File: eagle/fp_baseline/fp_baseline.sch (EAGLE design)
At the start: 6 parts, among them J5 TSM-105-01-S-SV

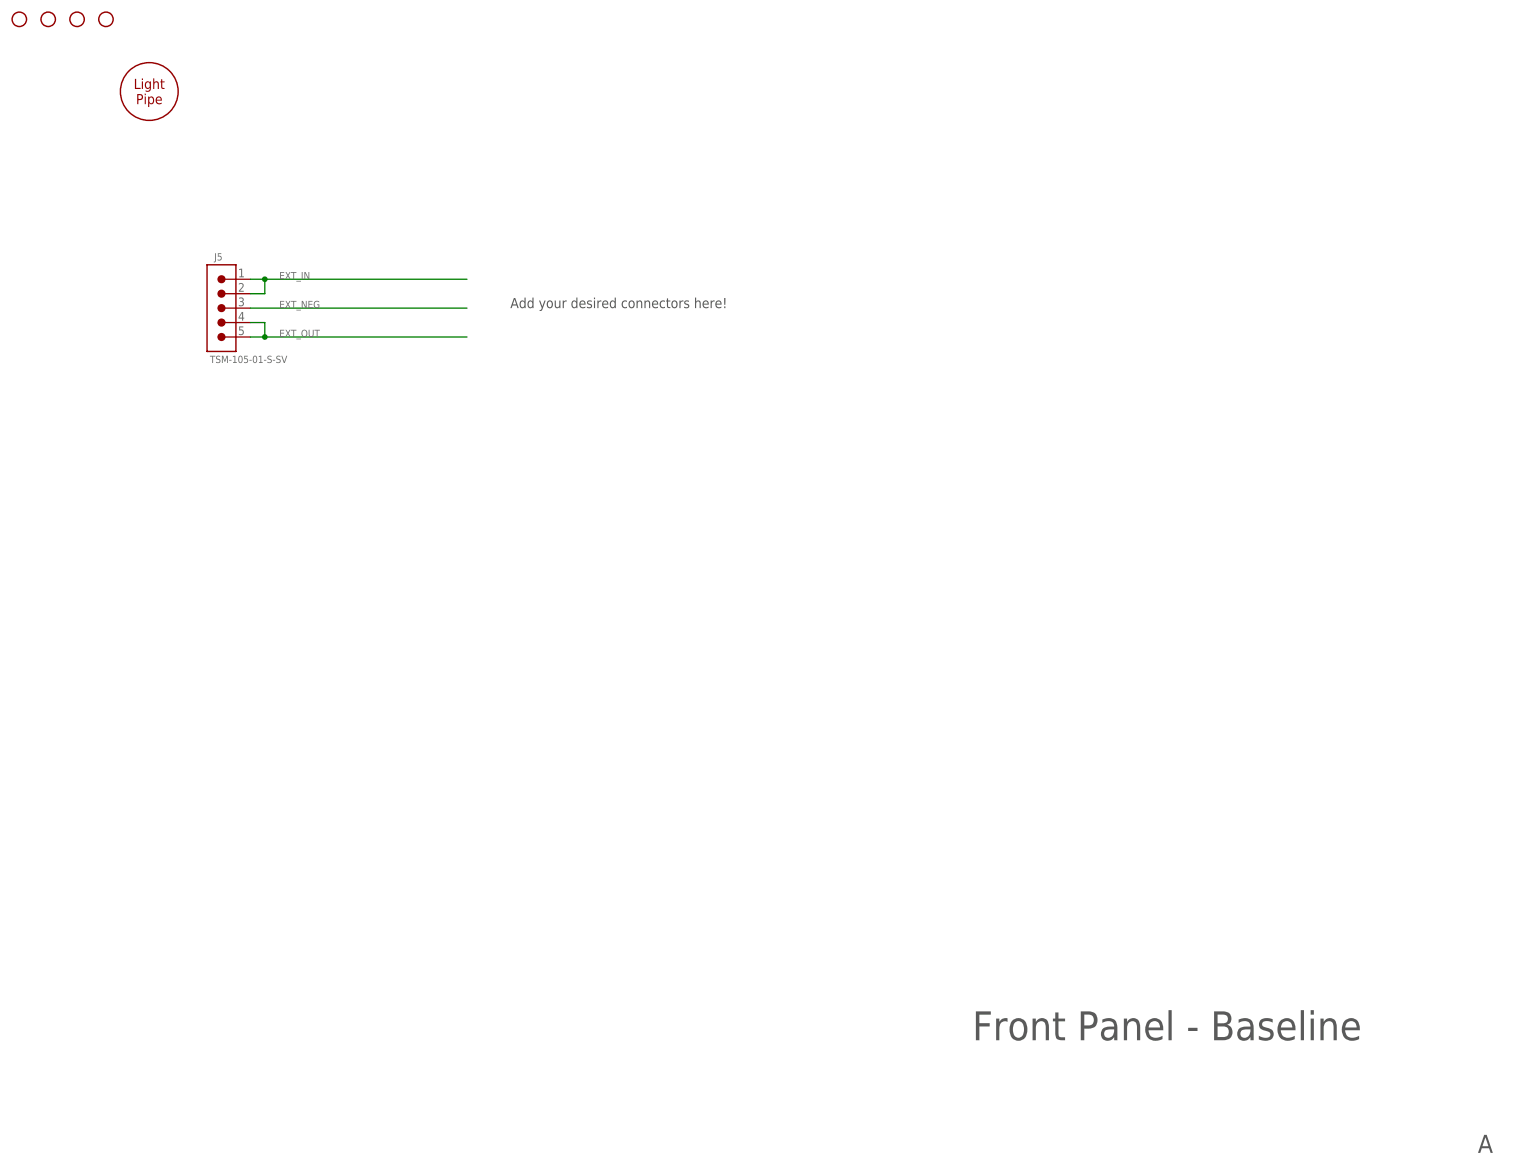
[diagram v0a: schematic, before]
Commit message: Updated baseline to clarify dimensions, placement and part numbers.
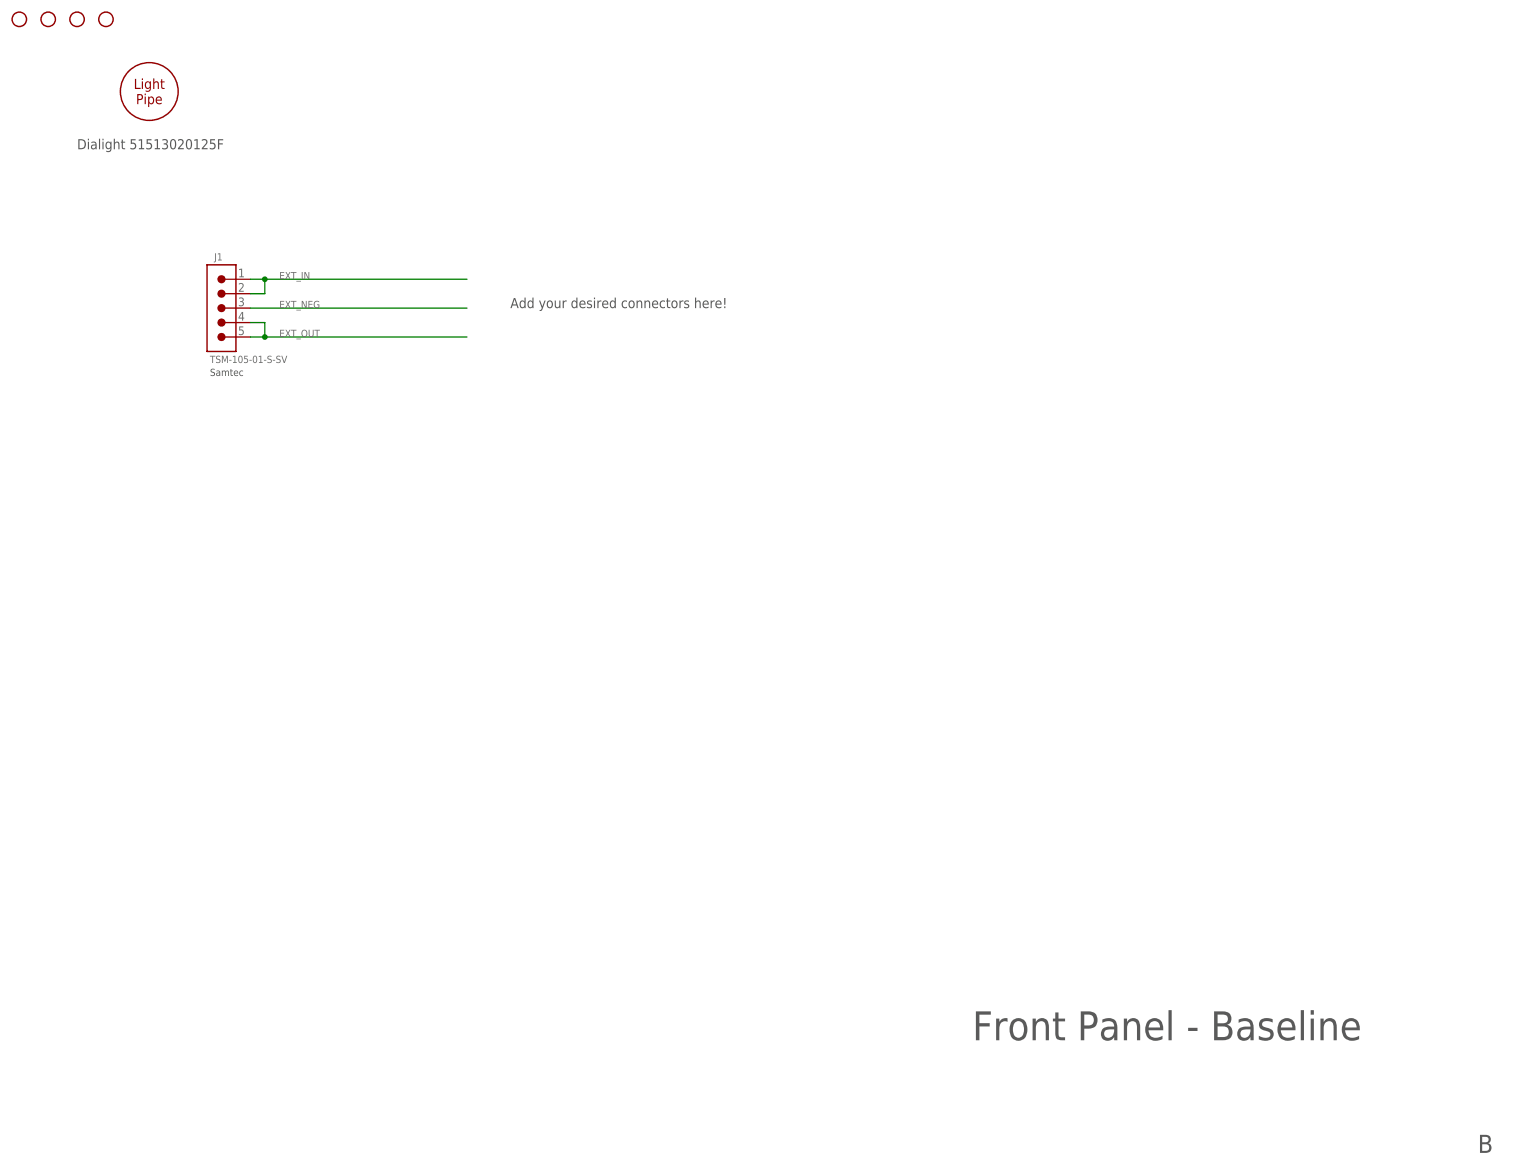
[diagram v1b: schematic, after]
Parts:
- renumbered J5 to J1
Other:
- note added: "B"
- note added: "Dialight 51513020125F"
- note added: "Samtec"
- note removed: "A"
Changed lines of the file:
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@@
 <?xml version="1.0" encoding="utf-8"?>
 <!DOCTYPE eagle SYSTEM "eagle.dtd">
-<eagle version="9.2.2">
+<eagle version="9.4.2">
 <drawing>
 <settings>
@@
 <parts>
 <part name="FRAME1" library="frames" library_urn="urn:adsk.eagle:library:229" deviceset="FRAME_A_L" device="" value="PG1"/>
-<part name="J5" library="jetperch" deviceset="CONN_0.1_5X1" device="_MS" value="TSM-105-01-S-SV">
+<part name="J1" library="jetperch" deviceset="CONN_0.1_5X1" device="_MS" value="TSM-105-01-S-SV">
 <attribute name="MPN" value="TSM-105-01-S-SV"/>
 <attribute name="POPULATE" value="1"/>
@@
 <attribute name="POPULATE" value="0"/>
 </part>
+<part name="H5" library="jetperch" deviceset="HOLE" device="_#6">
+<attribute name="POPULATE" value="0"/>
+</part>
 <part name="H4" library="jetperch" deviceset="HOLE" device="_#6">
-<attribute name="POPULATE" value="0"/>
-</part>
-<part name="H5" library="jetperch" deviceset="HOLE" device="_#6">
 <attribute name="POPULATE" value="0"/>
 </part>
@@
 <plain>
 <text x="177.8" y="26.162" size="5.08" layer="97">Front Panel - Baseline</text>
-<text x="266.7" y="6.35" size="3.175" layer="97">A</text>
+<text x="266.7" y="6.35" size="3.175" layer="97">B</text>
 <text x="96.52" y="154.94" size="1.778" layer="97">Add your desired connectors here!</text>
+<text x="20.32" y="182.88" size="1.778" layer="97">Dialight 51513020125F</text>
+<text x="43.688" y="143.002" size="1.27" layer="97">Samtec</text>
 </plain>
 <instances>
@@
 <attribute name="DRAWING_NAME" x="190.5" y="19.05" size="2.54" layer="94"/>
 </instance>
-<instance part="J5" gate="G$1" x="45.72" y="154.94" smashed="yes">
+<instance part="J1" gate="G$1" x="45.72" y="154.94" smashed="yes">
 <attribute name="MPN" x="45.72" y="154.94" size="1.778" layer="96" display="off"/>
 <attribute name="POPULATE" x="45.72" y="154.94" size="1.778" layer="96" display="off"/>
@@
 </instance>
 <instance part="H1" gate="G$1" x="33.02" y="193.04" smashed="yes"/>
-<instance part="H3" gate="G$1" x="10.16" y="205.74" smashed="yes">
+<instance part="H3" gate="G$1" x="15.24" y="205.74" smashed="yes">
+<attribute name="POPULATE" x="15.24" y="205.74" size="1.778" layer="96" display="off"/>
+</instance>
+<instance part="H2" gate="G$1" x="10.16" y="205.74" smashed="yes">
 <attribute name="POPULATE" x="10.16" y="205.74" size="1.778" layer="96" display="off"/>
 </instance>
-<instance part="H2" gate="G$1" x="15.24" y="205.74" smashed="yes">
-<attribute name="POPULATE" x="15.24" y="205.74" size="1.778" layer="96" display="off"/>
+<instance part="H5" gate="G$1" x="25.4" y="205.74" smashed="yes">
+<attribute name="POPULATE" x="25.4" y="205.74" size="1.778" layer="96" display="off"/>
 </instance>
 <instance part="H4" gate="G$1" x="20.32" y="205.74" smashed="yes">
 <attribute name="POPULATE" x="20.32" y="205.74" size="1.778" layer="96" display="off"/>
-</instance>
-<instance part="H5" gate="G$1" x="25.4" y="205.74" smashed="yes">
-<attribute name="POPULATE" x="25.4" y="205.74" size="1.778" layer="96" display="off"/>
 </instance>
 </instances>
@@
 <net name="EXT_IN" class="0">
 <segment>
-<pinref part="J5" gate="G$1" pin="2"/>
+<pinref part="J1" gate="G$1" pin="2"/>
 <wire x1="50.8" y1="157.48" x2="53.34" y2="157.48" width="0.1524" layer="91"/>
 <wire x1="53.34" y1="157.48" x2="53.34" y2="160.02" width="0.1524" layer="91"/>
-<pinref part="J5" gate="G$1" pin="1"/>
+<pinref part="J1" gate="G$1" pin="1"/>
 <wire x1="53.34" y1="160.02" x2="50.8" y2="160.02" width="0.1524" layer="91"/>
 <label x="55.88" y="160.02" size="1.27" layer="95"/>
@@
 <net name="EXT_NEG" class="0">
 <segment>
-<pinref part="J5" gate="G$1" pin="3"/>
+<pinref part="J1" gate="G$1" pin="3"/>
 <label x="55.88" y="154.94" size="1.27" layer="95"/>
 <wire x1="88.9" y1="154.94" x2="50.8" y2="154.94" width="0.1524" layer="91"/>
@@
 <net name="EXT_OUT" class="0">
 <segment>
-<pinref part="J5" gate="G$1" pin="5"/>
+<pinref part="J1" gate="G$1" pin="5"/>
 <wire x1="50.8" y1="149.86" x2="53.34" y2="149.86" width="0.1524" layer="91"/>
 <wire x1="53.34" y1="149.86" x2="53.34" y2="152.4" width="0.1524" layer="91"/>
-<pinref part="J5" gate="G$1" pin="4"/>
+<pinref part="J1" gate="G$1" pin="4"/>
 <wire x1="53.34" y1="152.4" x2="50.8" y2="152.4" width="0.1524" layer="91"/>
 <junction x="53.34" y="149.86"/>
